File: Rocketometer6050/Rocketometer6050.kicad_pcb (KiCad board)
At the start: 2 copper layers, 55.9 x 22.9 mm, 73 parts, among them J001 USB_MICROB, J301 JST 2mm, J401 M07, J701 Micro_SD_Card_Det_Hirose_DM3AT, Q050 PMOS, U101 BMP180, U201 3.3V, U301 MCP73831, U401 LPC2148, U601 MPU6050, U801 HMC5883L, U901 ADXL377, U902 AD7991, Y401 12MHz, Y402 32kiHz

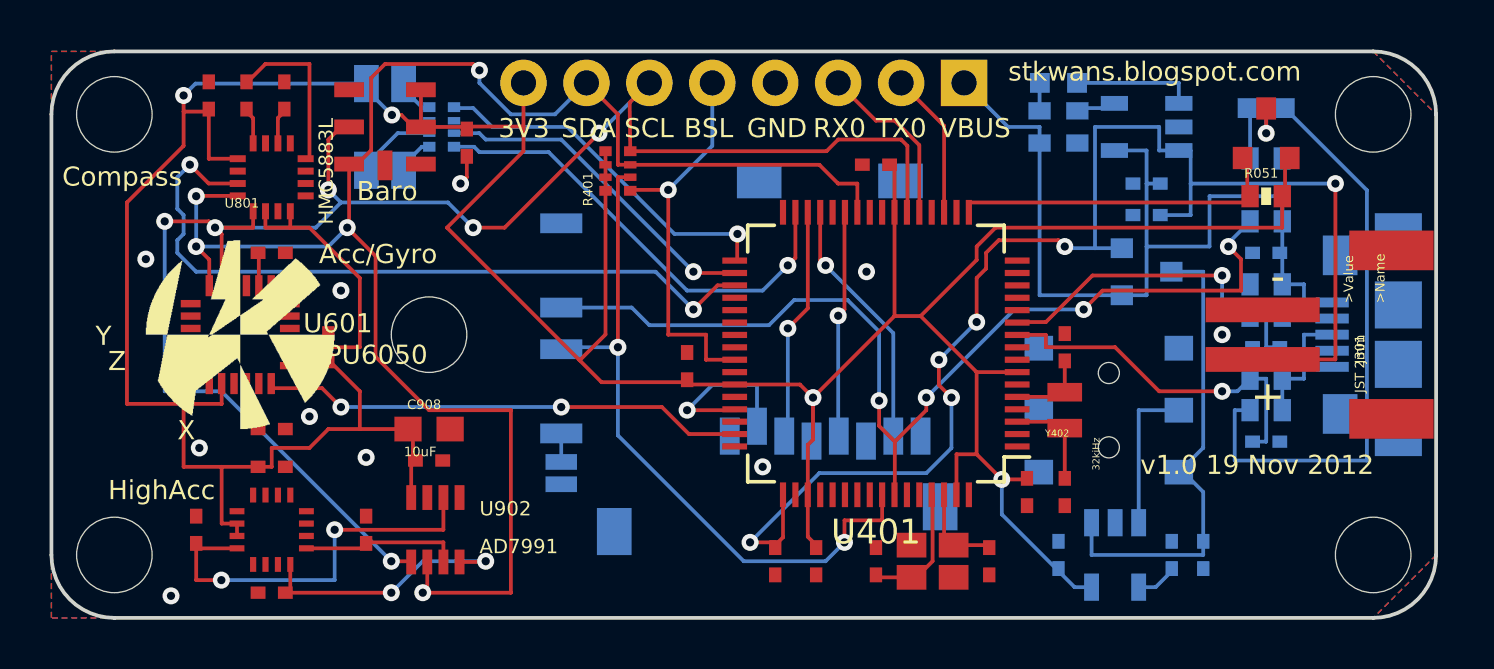
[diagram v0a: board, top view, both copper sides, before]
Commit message: Two "unconnected" airwires left. One is a ground connection which is actually through the case of the SD card, the other is through the case of the USB plug
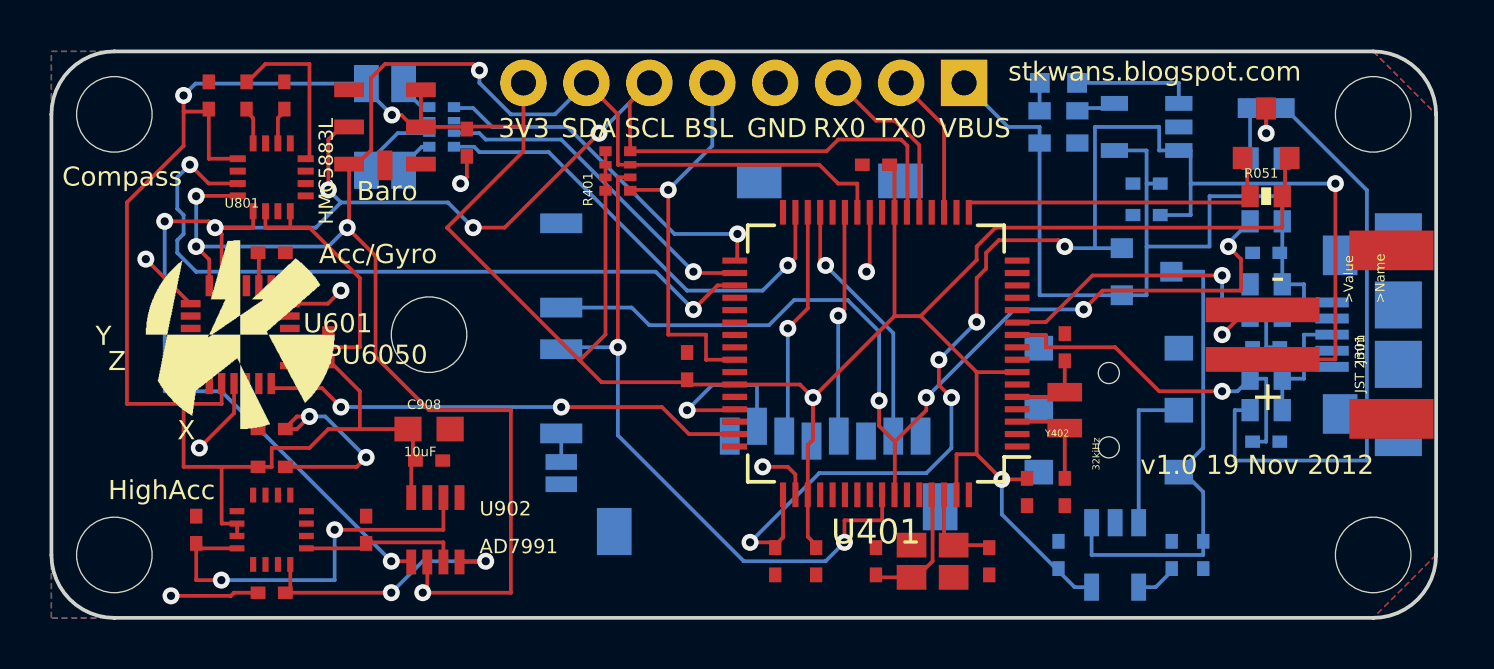
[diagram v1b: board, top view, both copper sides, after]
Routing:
- net GND: track 1.11 -> 28.5 mm
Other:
- net class Default: clearance 0 -> 0.1524
- rule trace_clearance: 0 -> 0.1524
